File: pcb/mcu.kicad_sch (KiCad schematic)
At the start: 6 parts, among them SW1 SW_DIP_x09, SW2 SW_DPDT_x2, U1 Teensy4.1, U2 SN65HVD11HD

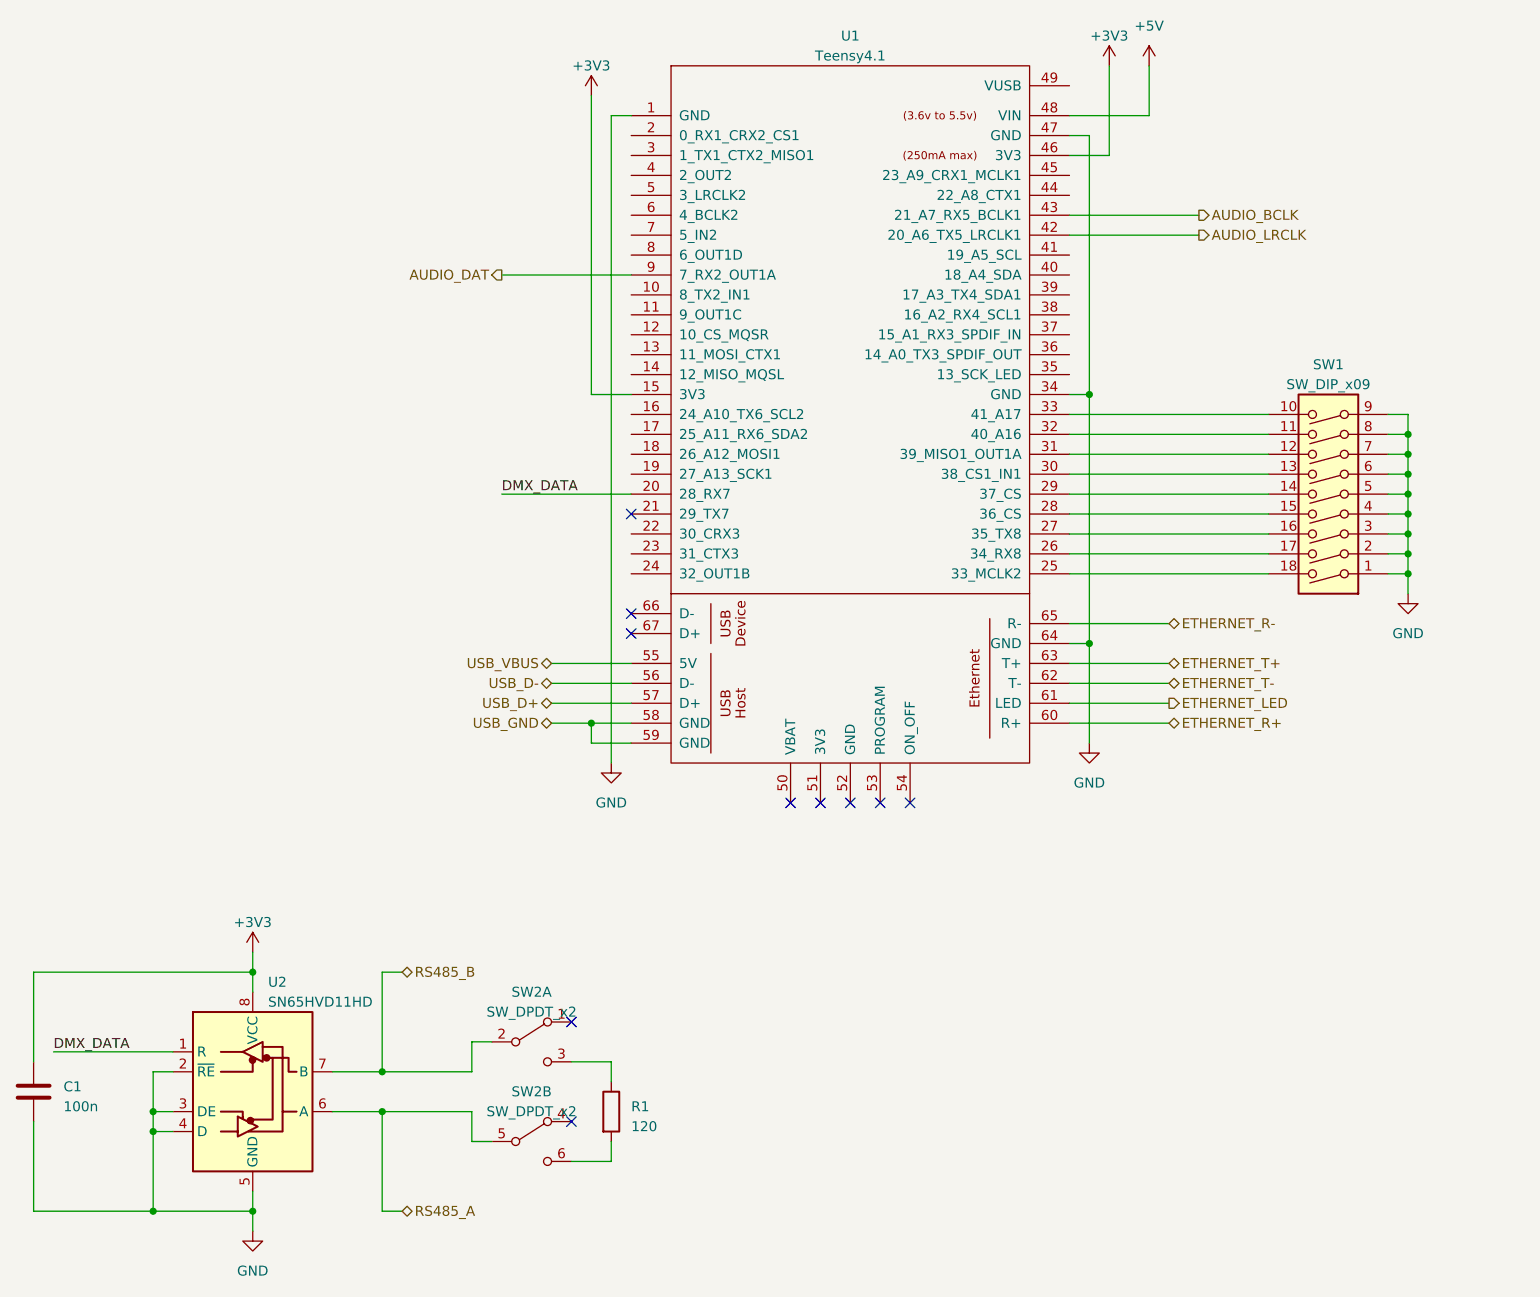
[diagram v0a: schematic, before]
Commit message: Updating schematic based on review from Mike
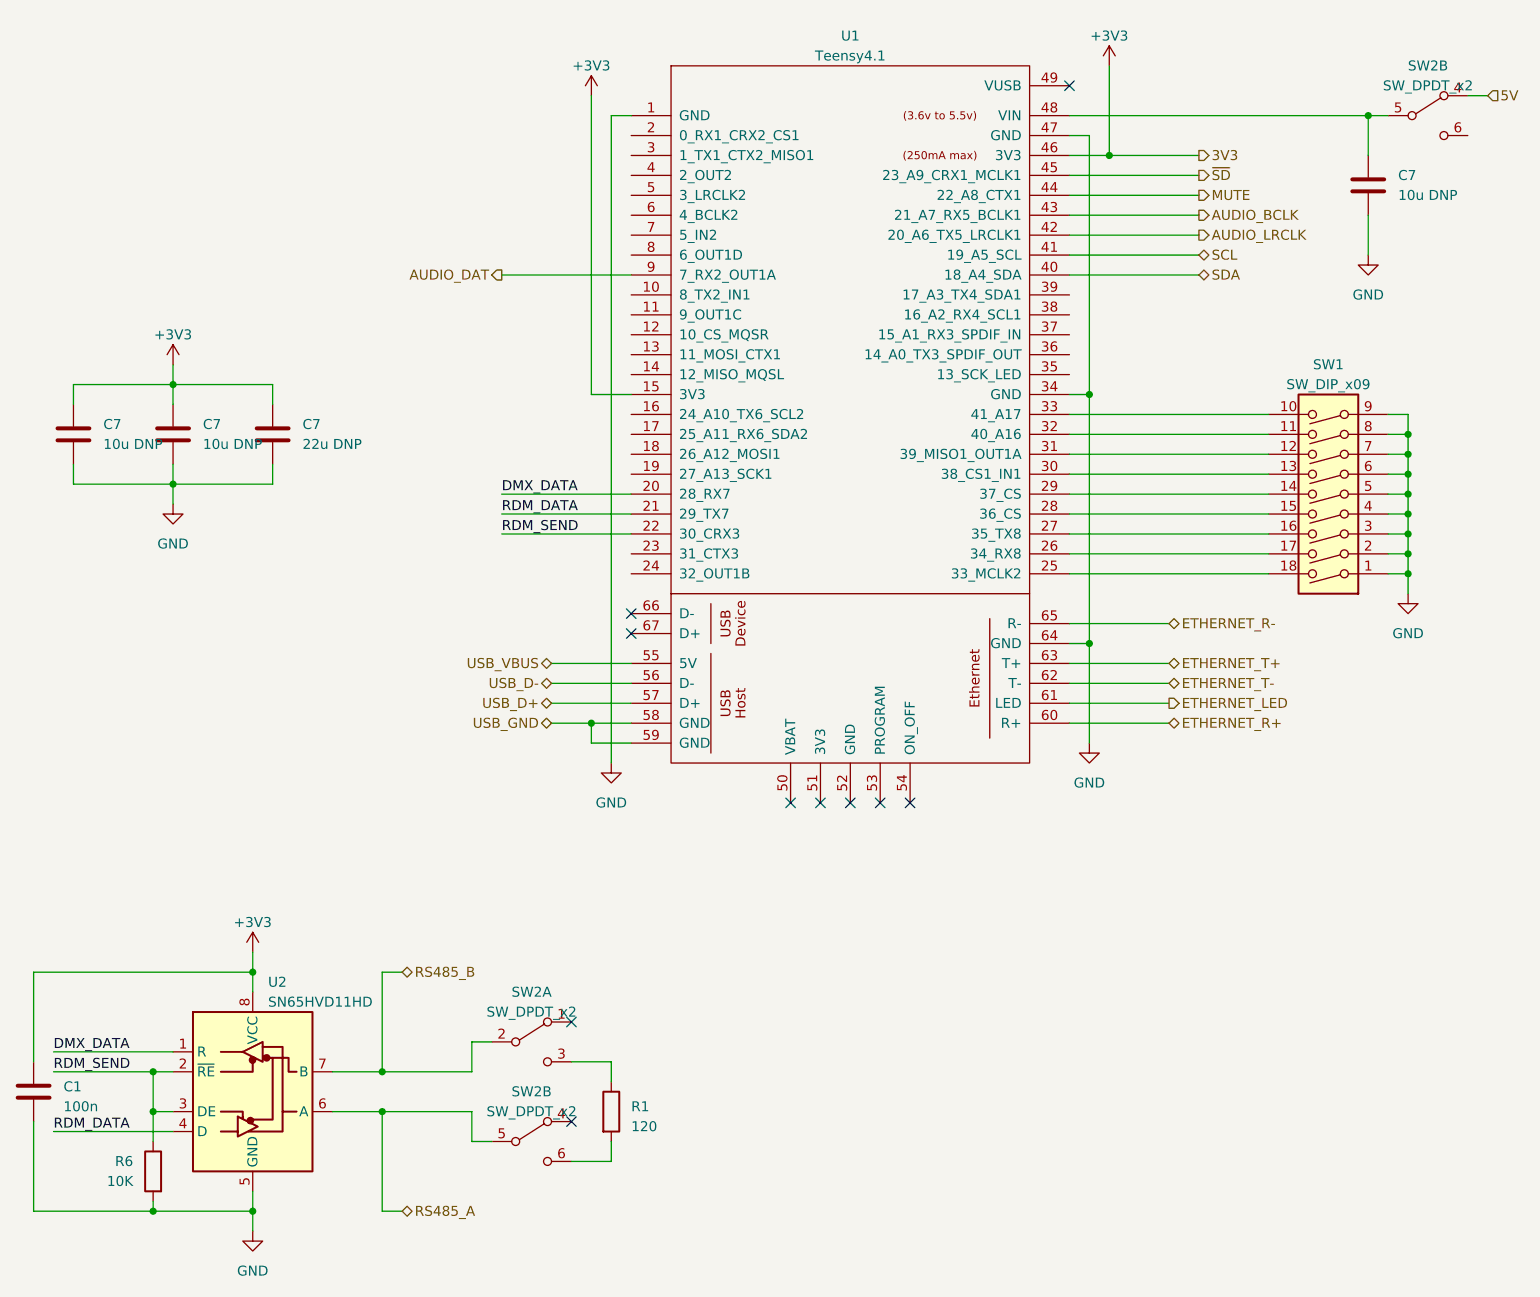
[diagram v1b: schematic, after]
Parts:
- added C7 (x3): 10u DNP, Capacitor_SMD:C_1206_3216Metric_Pad1.33x1.80mm_HandSolder, symbol Device:C
- added C7: 22u DNP, Capacitor_SMD:C_1206_3216Metric_Pad1.33x1.80mm_HandSolder, symbol Device:C
- added R6: 10K, Resistor_SMD:R_0603_1608Metric_Pad0.98x0.95mm_HandSolder, symbol Device:R
- added SW2: SW_DPDT_x2, Button_Switch_THT:SW_CuK_JS202011CQN_DPDT_Straight, symbol Switch:SW_DPDT_x2
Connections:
- net +3V3: now also C7.1, C7.1, C7.1
- net GND: now also C7.2, C7.2, C7.2, C7.2, R6.2; no longer U2.2 (~{RE}), U2.3 (DE), U2.4 (D)
- net RDM_DATA: now reaches U1.21 (29_TX7)
- net RDM_DATA: now also U2.4 (D)
- net RDM_SEND: now reaches U1.22 (30_CRX3)
- net RDM_SEND: now also U2.2 (~{RE}), U2.3 (DE), R6.1
- net SDA: now reaches U1.40 (18_A4_SDA)
- net SCL: now reaches U1.41 (19_A5_SCL)
- net MUTE: now reaches U1.44 (22_A8_CTX1)
- net ~{SD}: now reaches U1.45 (23_A9_CRX1_MCLK1)
- net +5V: no longer names the net of U1.48 (VIN)
- net +5V: now also C7.1, SW2.5 (B)
- new net 5V: SW2.4 (A)
